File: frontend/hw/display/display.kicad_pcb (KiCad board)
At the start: 2 copper layers, 13 parts, among them J1 Conn_01x06, J2 Conn_02x17_Odd_Even, Q1 MMBT3904, Q2 MMBT3904, U1 ESP32-WROOM-32U, U3 CH340C, U5 AMS1117-3.3

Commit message: Add more connections.
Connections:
- J2 pad 1: unconnected-(J2-Pad1) -> CS
- J2 pad 2: unconnected-(J2-Pad2) -> RS
- J2 pad 23: unconnected-(J2-Pad23) -> BL
- J2 pad 24: unconnected-(J2-Pad24) -> +3V3
- J2 pad 25: unconnected-(J2-Pad25) -> +3V3
- J2 pad 26: unconnected-(J2-Pad26) -> GND
- J2 pad 27: unconnected-(J2-Pad27) -> GND
- J2 pad 3: unconnected-(J2-Pad3) -> WR
- J2 pad 4: unconnected-(J2-Pad4) -> RD
- J2 pad 5: unconnected-(J2-Pad5) -> RST
- U1 pad 13: RED -> CS
- U1 pad 14: unconnected-(U1-Pad14) -> WR
- U1 pad 16: GREEN -> RS
- U1 pad 23: unconnected-(U1-Pad23) -> BL
- U1 pad 24: unconnected-(U1-Pad24) -> RD
- U1 pad 26: BUZ2 -> RST
- U1 pad 37: unconnected-(U1-Pad37) -> D8
- U1 pad 8: SENSE -> unconnected-(U1-Pad8)

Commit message: Ready for routing.
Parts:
- added C1: 10u, Capacitor_SMD:C_0805_2012Metric, F.Cu at (124.7, 64.3)
- added C6: 47u, Capacitor_SMD:CP_Elec_10x10, F.Cu at (115.7, 68.7)
- J1: value Conn_01x06 -> Conn_01x04; footprint Connector_USB:USB_Micro-B_Molex-105017-0001 -> Connector_JST:JST_XH_B4B-XH-A_1x04_P2.50mm_Vertical
- moved U3 66.5 mm to (99.1, 105.2)
- moved Q1 62.2 mm to (94.7, 96.5)
- moved C5 56.2 mm to (109.0, 85.6)
- moved R6 56.2 mm to (109.0, 83.1)
- moved C2 56.2 mm to (113.0, 83.1)
- moved U5 47.3 mm to (96.8, 67.1)
- moved C3 40.4 mm to (115.3, 93.5)
- moved R5 35.9 mm to (99.1, 96.0)
- moved Q2 32.7 mm to (100.8, 87.1)
- moved J1 26.5 mm to (88.8, 109.7), turned to 180 degrees
- moved C4 20.7 mm to (114.0, 103.4)
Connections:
- J1 pad 4: unconnected-(J1-Pad4) -> GND
- J2 pad 29: unconnected-(J2-Pad29) -> MISO
- J2 pad 30: unconnected-(J2-Pad30) -> MOSI
- J2 pad 31: unconnected-(J2-Pad31) -> PEN
- J2 pad 33: unconnected-(J2-Pad33) -> T_CS
- J2 pad 34: unconnected-(J2-Pad34) -> CLK
- U1 pad 10: unconnected-(U1-Pad10) -> MISO
- U1 pad 11: unconnected-(U1-Pad11) -> CLK
- U1 pad 12: unconnected-(U1-Pad12) -> T_CS
- U1 pad 8: unconnected-(U1-Pad8) -> MOSI
- U1 pad 9: unconnected-(U1-Pad9) -> PEN

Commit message: Do more routing.
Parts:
- moved C1 46.7 mm to (91.4, 97.0), turned to -90 degrees
- moved C4 35.8 mm to (90.4, 76.5), turned to 90 degrees
- moved C2 28.9 mm to (93.5, 104.4), turned to 180 degrees
- moved C5 22.3 mm to (90.4, 73.2), turned to 90 degrees
- moved C3 17.2 mm to (99.1, 99.1), turned to 180 degrees
- moved R6 15.2 mm to (95.0, 89.2), turned to 90 degrees
- moved Q2 8.64 mm to (92.2, 87.4), turned to 180 degrees
- moved U5 7.89 mm to (96.3, 74.9)
- moved Q1 4.17 mm to (92.2, 93.2), turned to 180 degrees
- moved R5 4.13 mm to (95.0, 96.8), turned to 90 degrees
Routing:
- net GND: track 0.00 -> 105.3 mm, vias 0 -> 4
- net WR: track 0.00 -> 51.4 mm, vias 0 -> 1
- net CS: track 0.00 -> 40.9 mm, vias 0 -> 1
- net RS: track 0.00 -> 40.8 mm, vias 0 -> 1
- net CLK: track 0.00 -> 40.0 mm, vias 0 -> 2
- net MOSI: track 0.00 -> 39.8 mm, vias 0 -> 2
- net RD: track 0.00 -> 39.0 mm, vias 0 -> 1
- net PEN: track 0.00 -> 38.8 mm, vias 0 -> 2
- net MISO: track 0.00 -> 35.8 mm, vias 0 -> 2
- net T_CS: track 0.00 -> 35.6 mm
- net RST: track 0.00 -> 28.4 mm, vias 0 -> 1
- net ESP_TX: track 0.00 -> 28.3 mm
- net ESP_RX: track 0.00 -> 28.3 mm
- net IO0: track 0.00 -> 23.1 mm, vias 0 -> 2
- net Net-(Q2-Pad2): track 0.00 -> 23.0 mm, vias 0 -> 2
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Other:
- board outline added: 43.9 x 43.9 mm

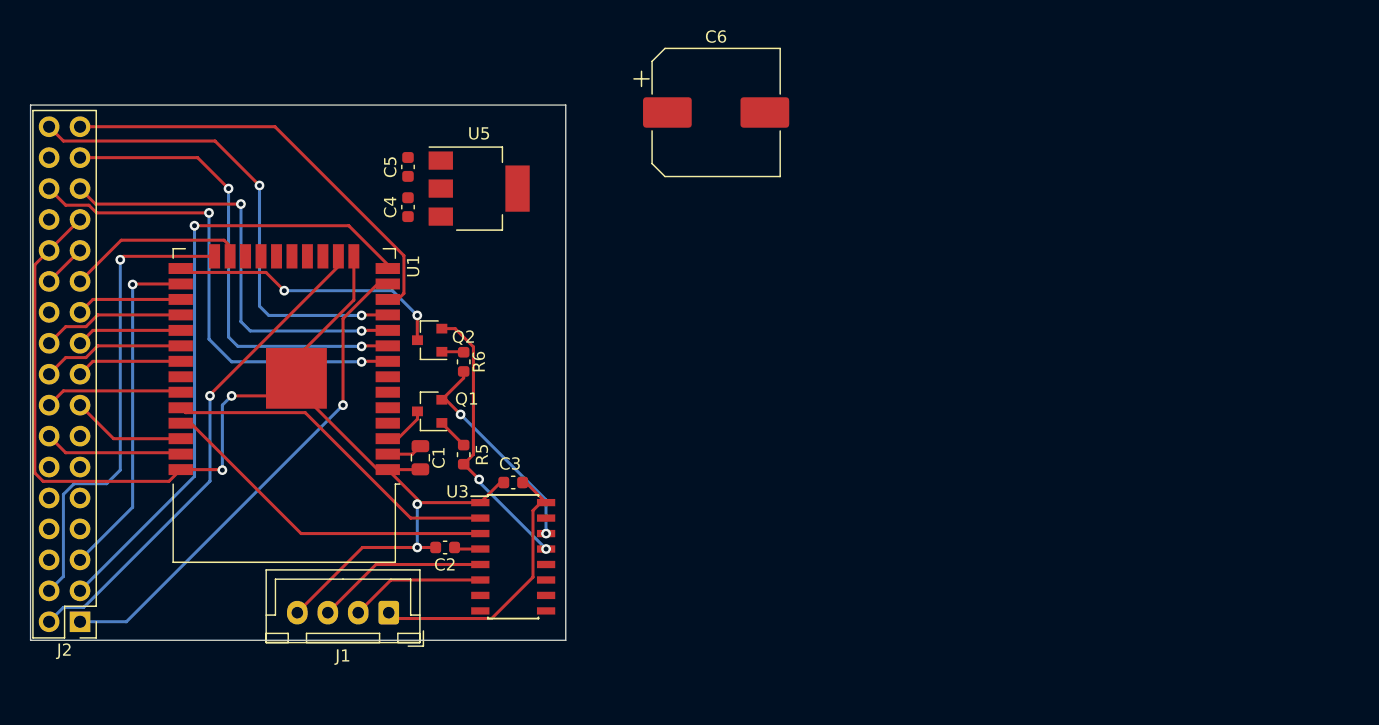
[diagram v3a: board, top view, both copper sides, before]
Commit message: Finish routing.
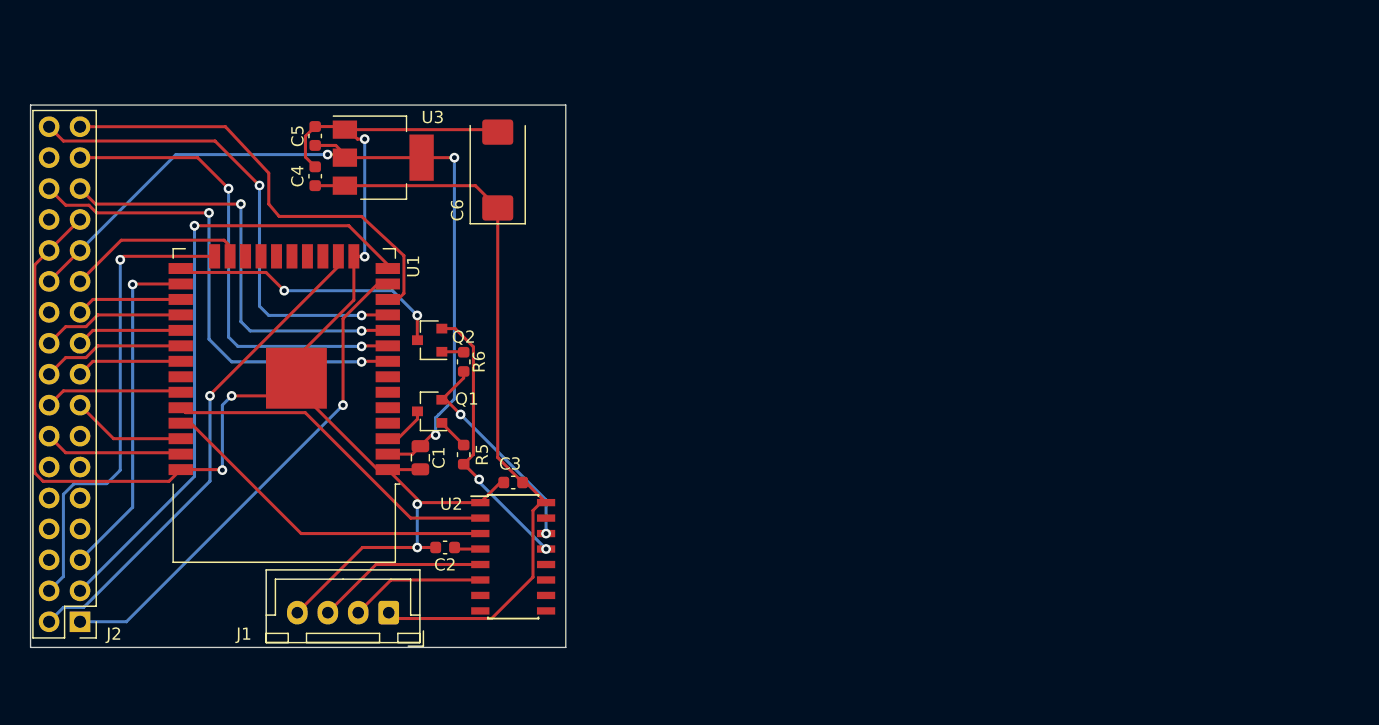
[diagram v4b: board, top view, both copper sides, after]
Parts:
- removed U5: AMS1117-3.3, Package_TO_SOT_SMD:SOT-223-3_TabPin2
- added U2: CH340C, Housings_SOIC:SOIC-16_3.9x9.9mm_Pitch1.27mm, F.Cu at (99.1, 105.2)
- C6: footprint Capacitor_SMD:CP_Elec_10x10 -> Capacitor_Tantalum_SMD:CP_EIA-7343-43_Kemet-X
- U3: value CH340C -> AMS1117-3.3; footprint Housings_SOIC:SOIC-16_3.9x9.9mm_Pitch1.27mm -> Package_TO_SOT_SMD:SOT-223-3_TabPin2
- moved U3 34.5 mm to (88.4, 72.4)
- moved C6 18.5 mm to (97.8, 73.4), turned to 90 degrees
- moved C5 8.03 mm to (82.8, 70.6)
- moved C4 8.03 mm to (82.8, 73.9)
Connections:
- J1 pad 2: Net-(J1-Pad2) -> Net-(U2-Pad6)
- J1 pad 3: Net-(J1-Pad3) -> Net-(U2-Pad5)
- U3 pad 2: ESP_RX -> +3V3
- U3 pad 3: ESP_TX -> +5V
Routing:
- net +3V3: track 6.54 -> 68.8 mm, vias 0 -> 3
- net +5V: track 22.9 -> 62.0 mm
- net GND: track 105.3 -> 136.7 mm, vias 4 -> 6
- net Net-(U2-Pad5): track 0.00 -> 14.2 mm
- net Net-(J1-Pad3): track 14.2 -> 0.00 mm
- net Net-(U2-Pad6): track 0.00 -> 11.1 mm
- net Net-(J1-Pad2): track 11.1 -> 0.00 mm
- net T_CS: track 35.6 -> 37.1 mm
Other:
- board size 43.9 x 43.9 mm -> 43.9 x 44.5 mm

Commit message: Add zones.
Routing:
- net +3V3: track 68.8 -> 72.4 mm
- net GND: track 136.7 -> 140.3 mm
- added copper zone on B.Cu, net +3V3
- added copper zone on B.Cu, net GND
- added copper zone on F.Cu, net GND
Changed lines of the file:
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@@
   (net 52 "D14")
   (net 53 "D15")
-  (net 54 "Net-(U2-Pad6)")
-  (net 55 "Net-(U2-Pad5)")
+  (net 54 "Net-(J1-Pad2)")
+  (net 55 "Net-(J1-Pad3)")
   (net 56 "unconnected-(U2-Pad7)")
   (net 57 "unconnected-(U2-Pad8)")
@@
       (net 1 "Net-(C2-Pad1)") (pinfunction "V3") (pintype "passive"))
     (pad "5" smd rect locked (at -2.7 0.635) (size 1.5 0.6) (layers "F.Cu" "F.Paste" "F.Mask")
-      (net 55 "Net-(U2-Pad5)") (pinfunction "UD+") (pintype "bidirectional"))
+      (net 55 "Net-(J1-Pad3)") (pinfunction "UD+") (pintype "bidirectional"))
     (pad "6" smd rect locked (at -2.7 1.905) (size 1.5 0.6) (layers "F.Cu" "F.Paste" "F.Mask")
-      (net 54 "Net-(U2-Pad6)") (pinfunction "UD-") (pintype "bidirectional"))
+      (net 54 "Net-(J1-Pad2)") (pinfunction "UD-") (pintype "bidirectional"))
     (pad "7" smd rect locked (at -2.7 3.175) (size 1.5 0.6) (layers "F.Cu" "F.Paste" "F.Mask")
       (net 56 "unconnected-(U2-Pad7)") (pinfunction "NC") (pintype "no_connect"))
@@
       (net 3 "+5V") (pinfunction "Pin_1") (pintype "passive"))
     (pad "2" thru_hole oval (at 2.5 0 180) (size 1.7 1.95) (drill 0.95) (layers *.Cu *.Mask)
-      (net 54 "Net-(U2-Pad6)") (pinfunction "Pin_2") (pintype "passive"))
+      (net 54 "Net-(J1-Pad2)") (pinfunction "Pin_2") (pintype "passive"))
     (pad "3" thru_hole oval (at 5 0 180) (size 1.7 1.95) (drill 0.95) (layers *.Cu *.Mask)
-      (net 55 "Net-(U2-Pad5)") (pinfunction "Pin_3") (pintype "passive"))
+      (net 55 "Net-(J1-Pad3)") (pinfunction "Pin_3") (pintype "passive"))
     (pad "4" thru_hole oval (at 7.5 0 180) (size 1.7 1.95) (drill 0.95) (layers *.Cu *.Mask)
       (net 2 "GND") (pinfunction "Pin_4") (pintype "passive"))
@@
   (segment (start 75.184 92.71) (end 75.946 91.948) (width 0.25) (layer "B.Cu") (net 2))
   (segment (start 86.868 80.518) (end 86.868 70.866) (width 0.25) (layer "B.Cu") (net 2))
+  (segment (start 60.96 80.01) (end 63.5 77.47) (width 0.25) (layer "B.Cu") (net 2))
   (segment (start 91.186 100.838) (end 91.186 104.394) (width 0.25) (layer "B.Cu") (net 2))
   (segment (start 100.685489 101.356489) (end 101.330978 100.711) (width 0.25) (layer "F.Cu") (net 3))
@@
   (segment (start 94.234 72.39) (end 94.234 92.202) (width 0.25) (layer "B.Cu") (net 4))
   (segment (start 94.234 92.202) (end 92.964 93.472) (width 0.25) (layer "B.Cu") (net 4))
+  (segment (start 60.96 82.55) (end 63.5 80.01) (width 0.25) (layer "B.Cu") (net 4))
   (segment (start 63.5 80.01) (end 71.374 72.136) (width 0.25) (layer "B.Cu") (net 4))
   (segment (start 92.693452 93.742548) (end 92.693452 95.164636) (width 0.25) (layer "B.Cu") (net 4))
@@
   (segment (start 87.794 105.791) (end 83.84 109.745) (width 0.25) (layer "F.Cu") (net 55))
   (segment (start 96.36 105.791) (end 87.794 105.791) (width 0.25) (layer "F.Cu") (net 55))
+  (zone (net 2) (net_name "GND") (layer "F.Cu") (hatch edge 0.508)
+    (connect_pads (clearance 1))
+    (min_thickness 0.5) (filled_areas_thickness no)
+    (fill yes (thermal_gap 0.508) (thermal_bridge_width 0.508))
+    (polygon
+      (pts
+        (xy 103.378 112.522)
+        (xy 59.182 112.268)
+        (xy 59.182 68.072)
+        (xy 103.378 68.072)
+      )
+    )
+  )
+  (zone (net 2) (net_name "GND") (layer "B.Cu") (hatch edge 0.508)
+    (connect_pads (clearance 0.508))
+    (min_thickness 0.254) (filled_areas_thickness no)
+    (fill yes (thermal_gap 0.508) (thermal_bridge_width 0.508))
+    (polygon
+      (pts
+        (xy 103.632 112.776)
+        (xy 68.072 112.776)
+        (xy 68.326 110.744)
+        (xy 78.74 100.584)
+        (xy 103.632 100.584)
+      )
+    )
+  )
+  (zone (net 4) (net_name "+3V3") (layer "B.Cu") (hatch edge 0.508)
+    (connect_pads (clearance 0.508))
+    (min_thickness 0.254) (filled_areas_thickness no)
+    (fill yes (thermal_gap 0.508) (thermal_bridge_width 0.508))
+    (polygon
+      (pts
+        (xy 85.09 73.66)
+        (xy 73.66 73.66)
+        (xy 64.008 83.82)
+        (xy 58.928 83.566)
+        (xy 58.928 67.564)
+        (xy 85.09 67.564)
+      )
+    )
+  )
+  (zone (net 4) (net_name "+3V3") (layer "B.Cu") (hatch edge 0.508)
+    (connect_pads (clearance 0.508))
+    (min_thickness 0.254) (filled_areas_thickness no)
+    (fill yes (thermal_gap 0.508) (thermal_bridge_width 0.508))
+    (polygon
+      (pts
+        (xy 103.378 100.076)
+        (xy 90.424 99.822)
+        (xy 90.424 68.072)
+        (xy 103.378 68.072)
+      )
+    )
+  )
 )

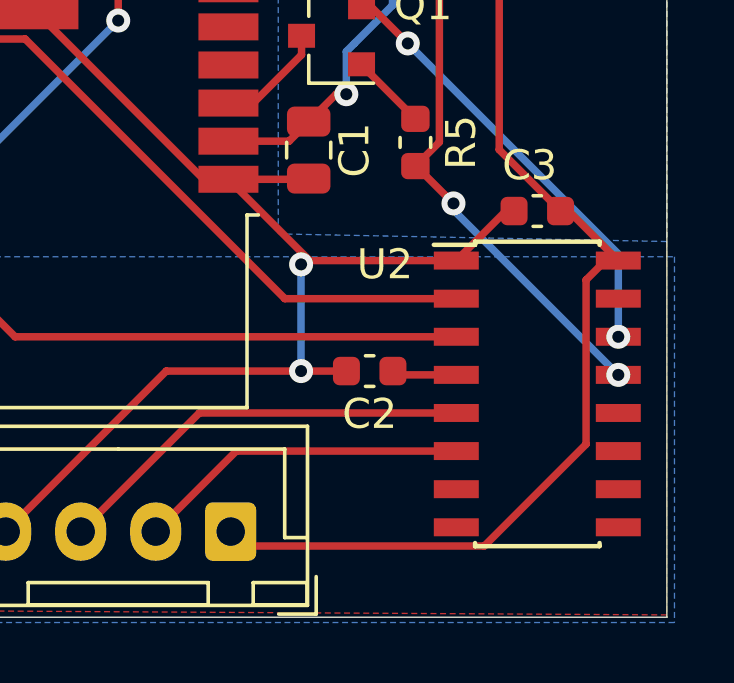
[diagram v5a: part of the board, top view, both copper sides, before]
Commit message: Fix 3D view.
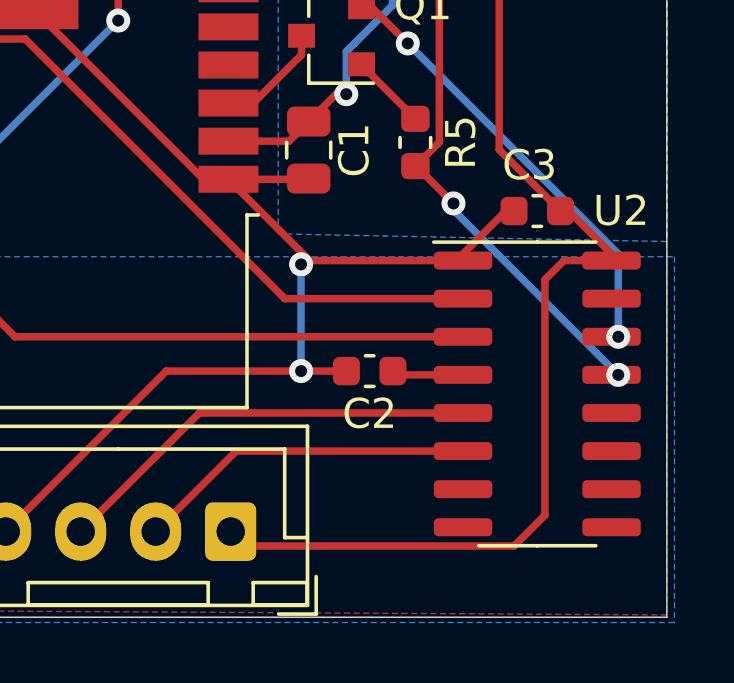
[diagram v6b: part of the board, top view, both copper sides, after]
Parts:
- U2: footprint Housings_SOIC:SOIC-16_3.9x9.9mm_Pitch1.27mm -> Package_SO:SOIC-16_3.9x9.9mm_P1.27mm
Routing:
- net +5V: track 62.0 -> 63.6 mm
